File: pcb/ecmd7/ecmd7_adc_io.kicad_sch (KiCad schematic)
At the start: 73 parts, among them U10 FIN1002M5X, U11 FIN1002M5X, U12 FIN1002M5X, U13 ADM3490ExR, U2 MCP33151-05T-E/MN, U4 MCP33151-05T-E/MN, U5 MCP33151-05T-E/MN, U7 MCP33151-05T-E/MN

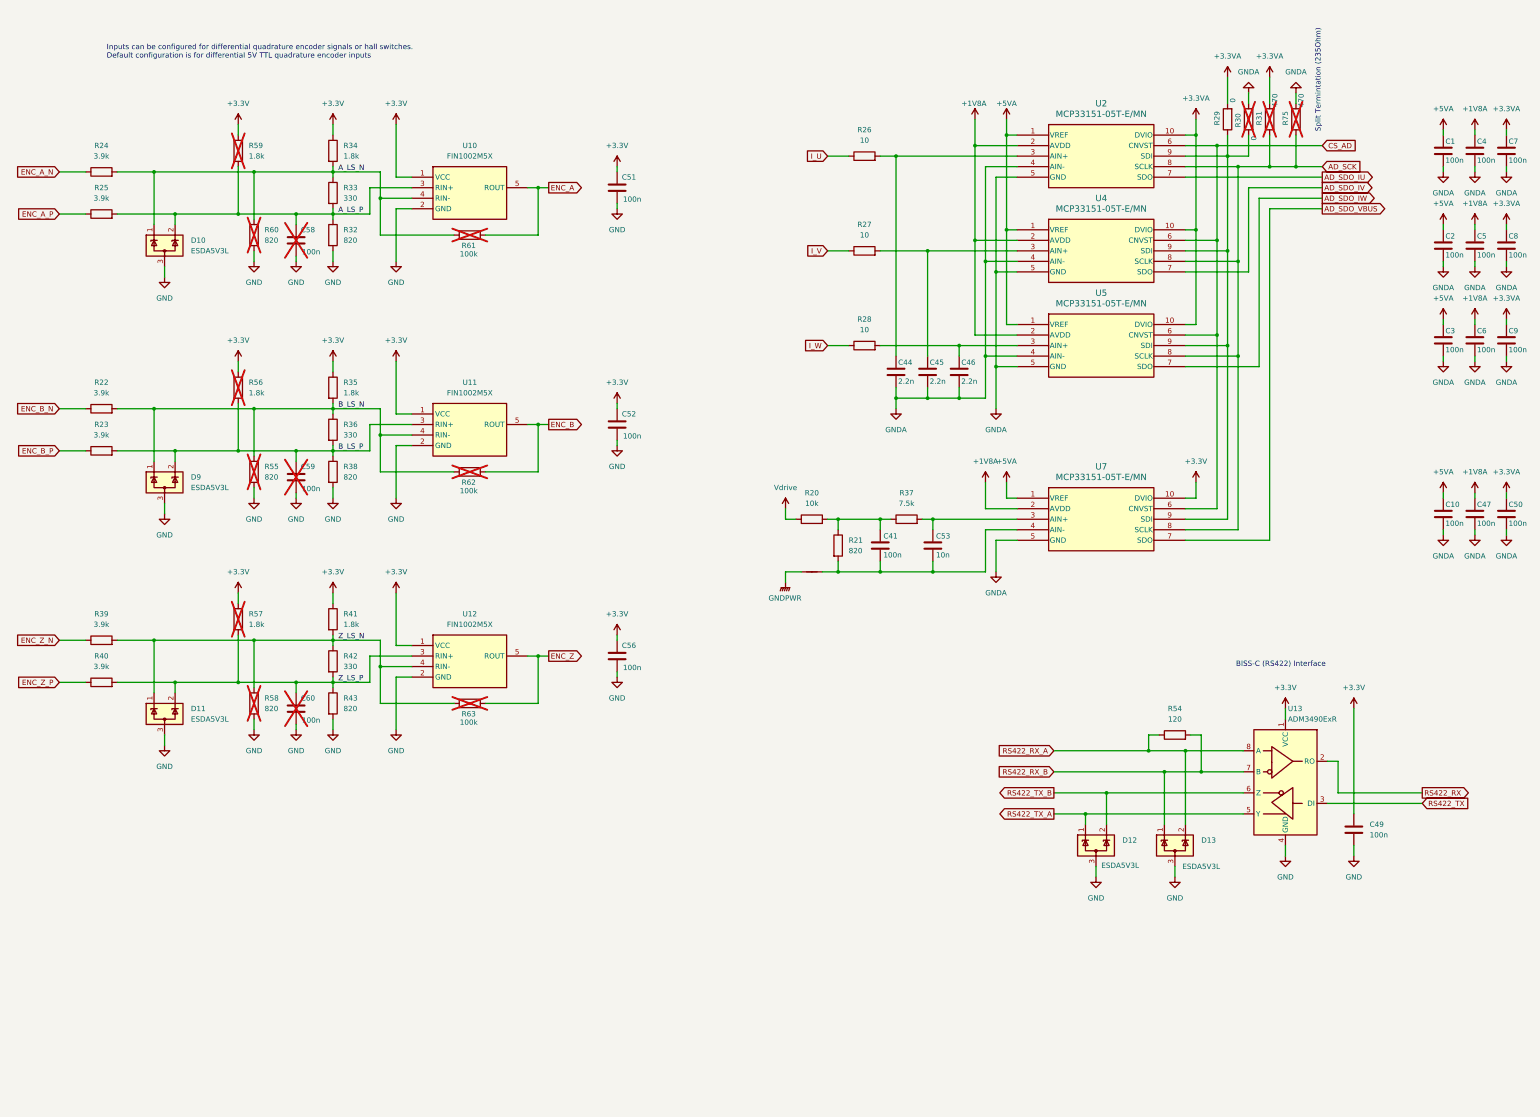
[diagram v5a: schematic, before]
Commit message: Routing complete, DRC successful
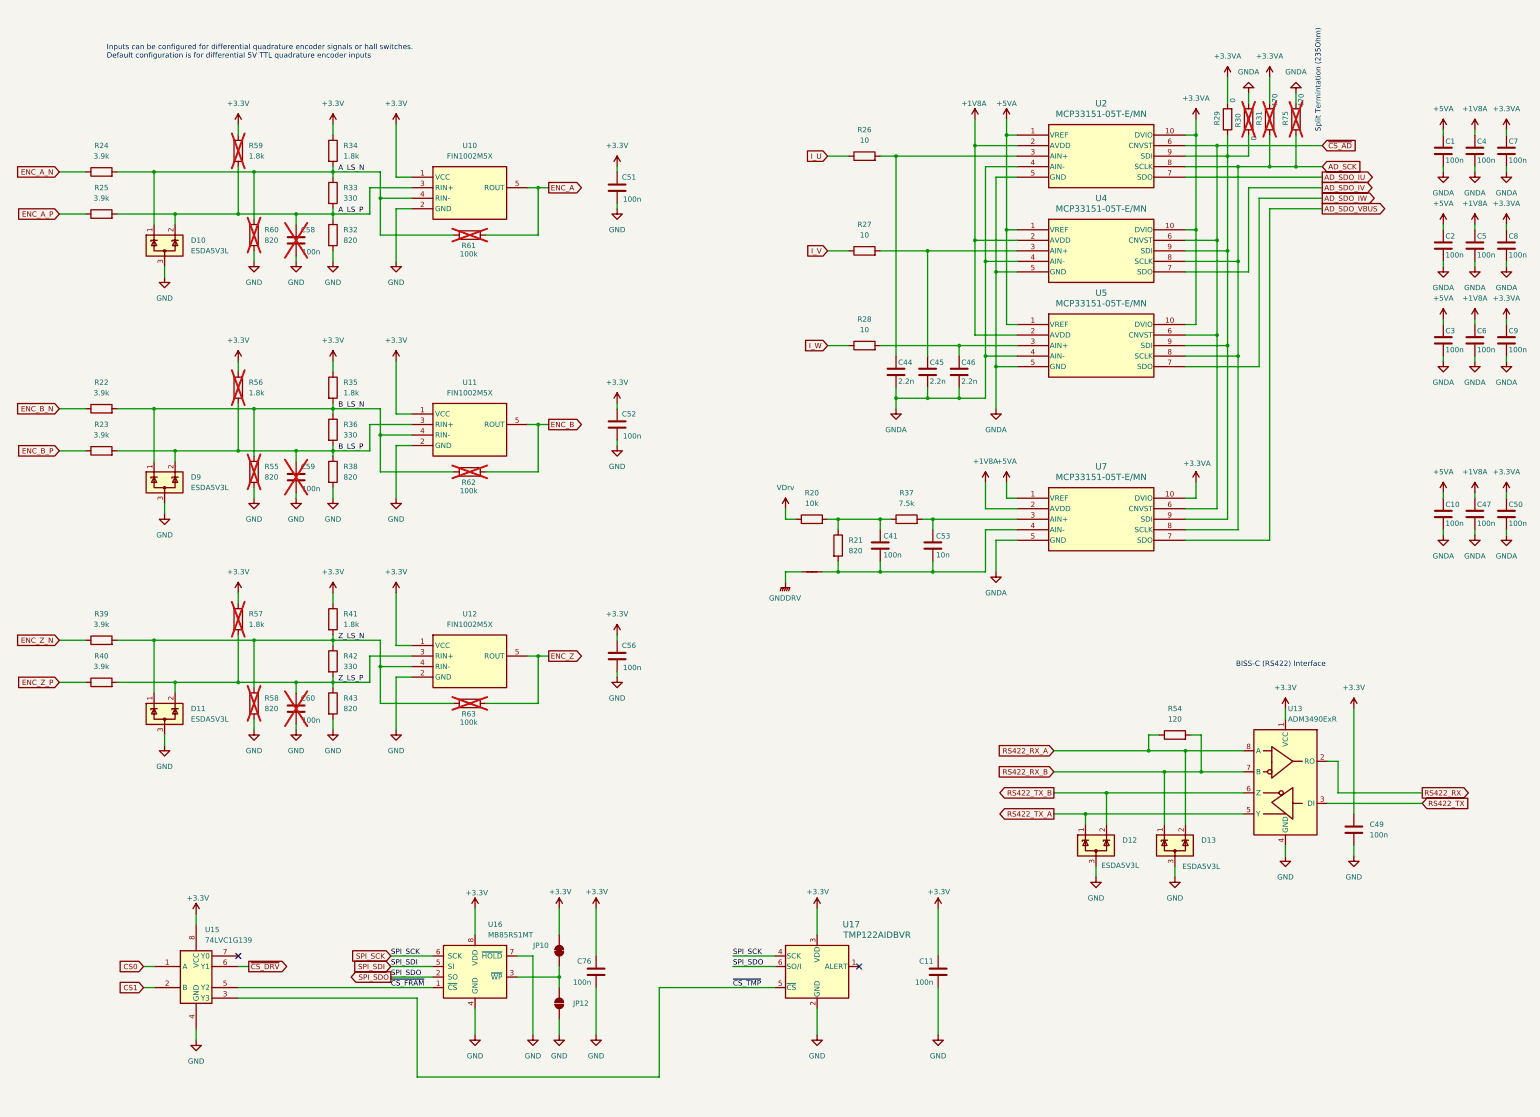
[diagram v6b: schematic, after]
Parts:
- added C11, C76: 100n, Capacitor_SMD:C_0805_2012Metric, symbol Device:C
- added JP10: SolderJumper_2_Bridged, Jumper:SolderJumper-2_P1.3mm_Bridged_RoundedPad1.0x1.5mm, symbol Jumper:SolderJumper_2_Bridged
- added JP12: SolderJumper_2_Open, Jumper:SolderJumper-2_P1.3mm_Open_RoundedPad1.0x1.5mm, symbol Jumper:SolderJumper_2_Open
- added U15: 74LVC1G139, Package_SO:SSOP-8_2.95x2.8mm_P0.65mm, symbol 74xGxx:74LVC1G139
- added U16: MB85RS1MT, Package_SO:SOP-8_3.76x4.96mm_P1.27mm, symbol Memory_NVRAM:MB85RS1MT
- added U17: TMP122AIDBVR, SSTA:DBV6, symbol SSTA:TMP122AIDBVR
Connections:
- net +3.3V: now also C11.1, C76.1, JP10.2 (B), U15.8 (VCC), U16.8 (VDD), U17.3 (VDD); no longer U7.10 (DVIO)
- net +3.3VA: now also U7.10 (DVIO)
- net GND: now also C11.2, C76.2, JP12.1 (A), U15.4 (GND), U16.4 (GND), U16.7 (~{HOLD}), U17.2 (GND)
- net CS_AD renamed ~{CS_AD}
- net GNDPWR renamed GNDDRV
- net Vdrive renamed VDrv
- new net: JP10.1 (A), JP12.2 (B), U16.3 (~{WP})
- new net CS0: U15.1 (A)
- new net CS1: U15.2 (B)
- new net SPI_SCK: U16.6 (SCK), U17.4 (SCK)
- new net SPI_SDI: U16.5 (SI)
- new net SPI_SDO: U16.2 (SO), U17.6 (SO/I)
- new net ~{CS_DRV}: U15.6 (Y1)
- new net ~{CS_FRAM}: U15.5 (Y2), U16.1 (~{CS})
- new net ~{CS_TMP}: U15.3 (Y3), U17.5 (~{CS})
- no-connect marks 0 -> 2

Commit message: Final layout
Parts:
- added R49, R53, R76, R9: 330, Resistor_SMD:R_0805_2012Metric, symbol Device:R
- JP10: value SolderJumper_2_Bridged -> ~{WP}=1
- JP12: value SolderJumper_2_Open -> ~{WP}=0
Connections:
- net +3.3V: now also R53.1, R9.1
- net GND: now also R49.2, R76.2
- net SPI_SCK: now also R53.2, R76.1
- net SPI_SDI: now also R49.1, R9.2
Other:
- moved on the sheet: C11, C76, JP10, JP12, U15, U16, U17
